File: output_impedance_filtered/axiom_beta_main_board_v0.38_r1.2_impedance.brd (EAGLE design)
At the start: 111.8 x 57.1 mm, 0 parts

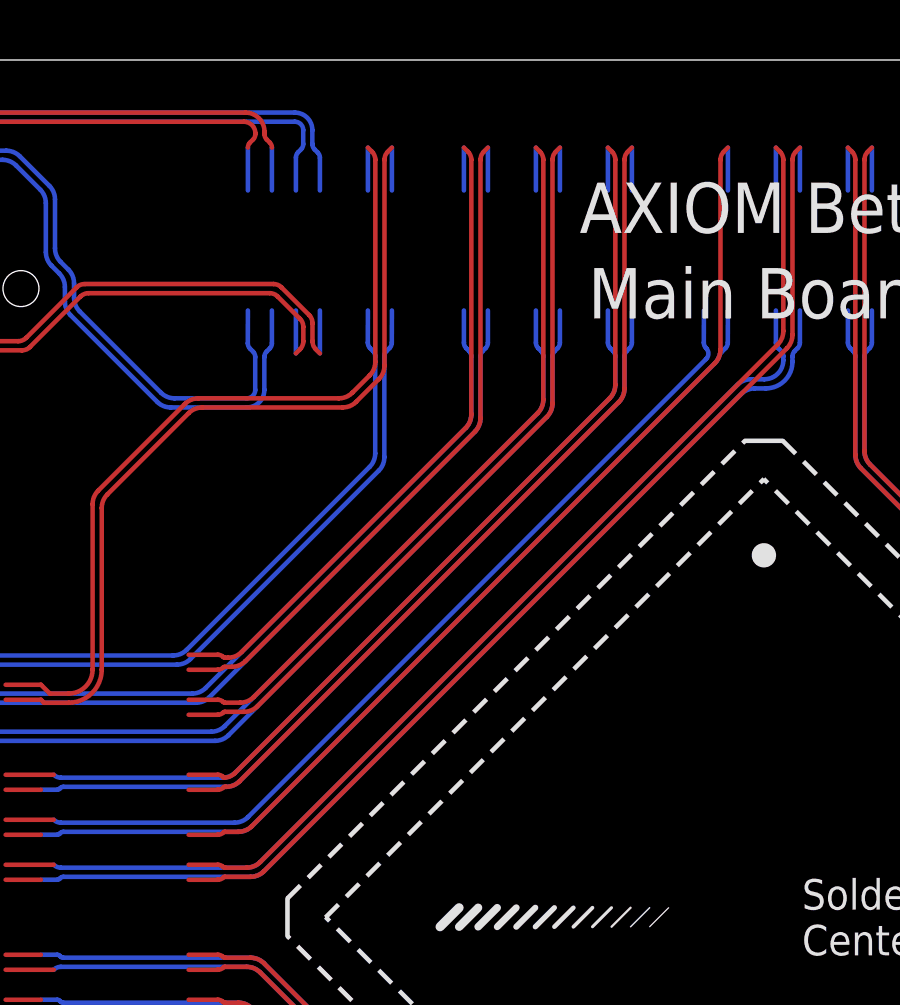
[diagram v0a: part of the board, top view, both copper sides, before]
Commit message: new impedance filtering update
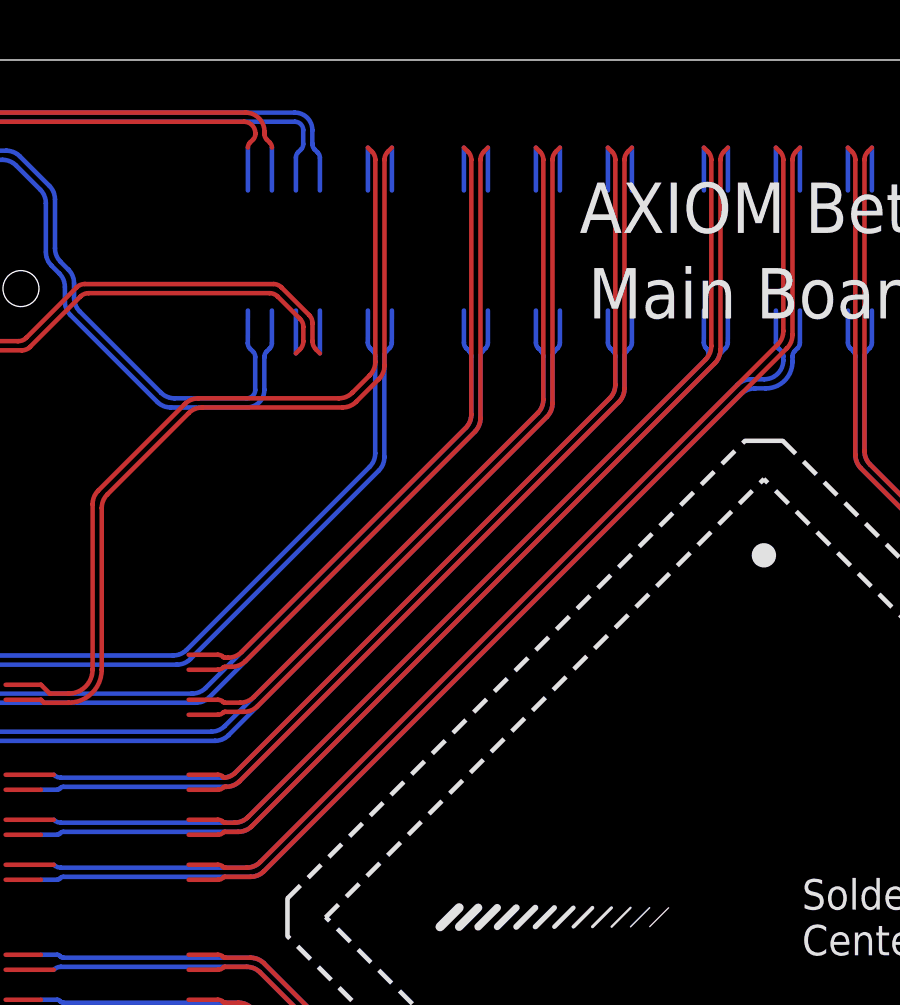
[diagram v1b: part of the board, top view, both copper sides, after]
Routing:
- net JX1_14_N: track 0.00 -> 32.2 mm
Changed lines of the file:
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@@
 <setting verticaltext="up"/>
 </settings>
-<grid distance="0.5" unitdist="mm" unit="mm" style="lines" multiple="1" display="yes" altdistance="0.1" altunitdist="mm" altunit="mm"/>
+<grid distance="0.05" unitdist="inch" unit="inch" style="lines" multiple="1" display="yes" altdistance="0.025" altunitdist="inch" altunit="inch"/>
 <layers>
 <layer number="1" name="Top" color="16" fill="1" visible="yes" active="yes"/>
@@
 <wire x1="10.7383875" y1="13.60714375" x2="17.00714375" y2="7.3383875" width="0.1524" layer="1"/>
 </signal>
+<signal name="JX1_14_N" class="1">
+<wire x1="-2" y1="24.2258" x2="-2" y2="25.654" width="0.1524" layer="16"/>
+<wire x1="-2" y1="25.654" x2="-1.86399375" y2="25.51799375" width="0.1524" layer="1"/>
+<wire x1="-1.86399375" y1="25.51799375" x2="-1.7524" y2="25.248584375" width="0.1524" layer="1" curve="-45.00047"/>
+<wire x1="-18.02320625" y1="3.17560625" x2="-17.96718125" y2="3.1524" width="0.1524" layer="1" curve="45"/>
+<wire x1="-17.96718125" y1="3.1524" x2="-17.64615625" y2="3.1524" width="0.1524" layer="1"/>
+<wire x1="-18.02320625" y1="3.17560625" x2="-18.202809375" y2="3.25" width="0.1524" layer="1" curve="44.999295"/>
+<wire x1="-18.202809375" y1="3.25" x2="-19.175" y2="3.25" width="0.1524" layer="1"/>
+<wire x1="-17.64615625" y1="3.1524" x2="-17.19714375" y2="3.3383875" width="0.1524" layer="1" curve="45"/>
+<wire x1="-17.19714375" y1="3.3383875" x2="-1.9383875" y2="18.59714375" width="0.1524" layer="1"/>
+<wire x1="-1.9383875" y1="18.59714375" x2="-1.7524" y2="19.04615625" width="0.1524" layer="1" curve="45"/>
+<wire x1="-1.7524" y1="19.04615625" x2="-1.7524" y2="25.248584375" width="0.1524" layer="1"/>
+</signal>
 <signal name="JX2_15_P" class="1">
